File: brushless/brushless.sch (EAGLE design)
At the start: 71 parts, among them Q1 BUK7Y12-40E, Q2 BUK7Y12-40E, Q3 BUK7Y12-40E, Q4 BUK7Y12-40E, Q5 BUK7Y12-40E, Q6 BUK7Y12-40E, X2 MOTOR

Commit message: 0.25
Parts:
- UC1: device stm32:STM32F103CB -> rhoban:STM32_STM32F103CB
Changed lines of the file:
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@@
 <attribute name="FARNELL" value="1581233"/>
 </part>
-<part name="UC1" library="stm32" deviceset="STM32F103CB" device="" value="STM32F103CBT6">
+<part name="UC1" library="rhoban" deviceset="STM32_STM32F103CB" device="" value="STM32F103CBT6">
 <attribute name="FARNELL" value="1606327"/>
 </part>

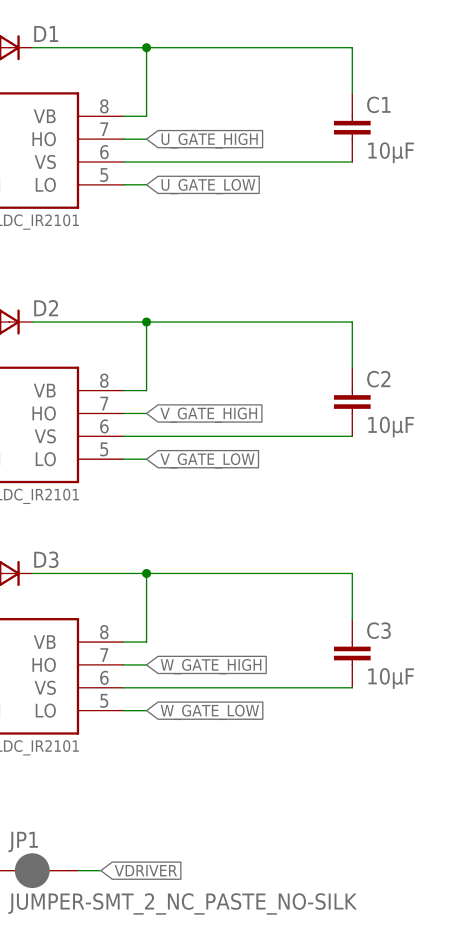
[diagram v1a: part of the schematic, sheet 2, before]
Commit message: Fixing phase on bootstrap capcaitors
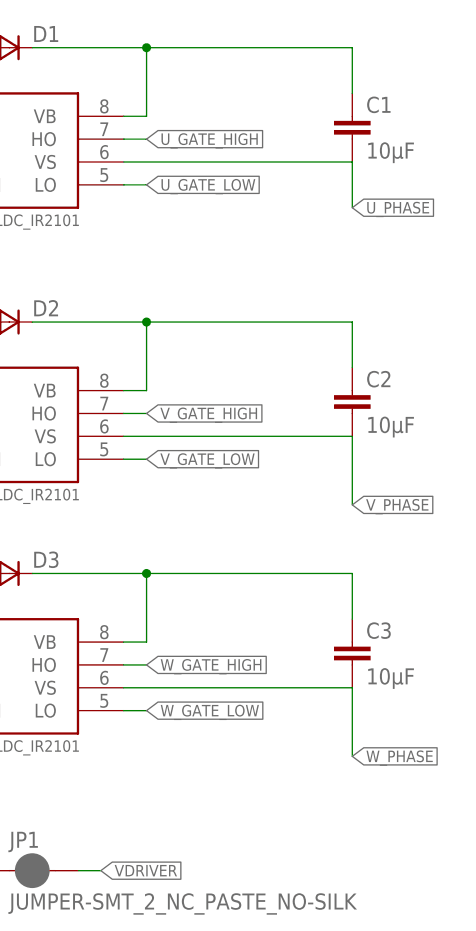
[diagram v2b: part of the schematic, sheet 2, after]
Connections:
- removed net N$11: C1.2, DRV1.VS
- removed net N$14: C2.2, DRV2.VS
- removed net N$18: C3.2, DRV3.VS
- net U_PHASE: now also C1.2, DRV1.VS
- net V_PHASE: now also C2.2, DRV2.VS
- net W_PHASE: now also C3.2, DRV3.VS
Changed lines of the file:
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@@
 </segment>
 </net>
-<net name="N$11" class="0">
+<net name="U_PHASE" class="2">
 <segment>
 <pinref part="C1" gate="G$1" pin="2"/>
 <pinref part="DRV1" gate="G$1" pin="VS"/>
 <wire x1="88.9" y1="78.74" x2="63.5" y2="78.74" width="0.1524" layer="91"/>
+<wire x1="88.9" y1="78.74" x2="88.9" y2="73.66" width="0.1524" layer="91"/>
+<label x="88.9" y="73.66" size="1.27" layer="95" xref="yes"/>
 </segment>
 </net>
@@
 </segment>
 </net>
-<net name="N$14" class="0">
+<net name="V_PHASE" class="2">
 <segment>
 <pinref part="C2" gate="G$1" pin="2"/>
 <pinref part="DRV2" gate="G$1" pin="VS"/>
 <wire x1="88.9" y1="48.26" x2="63.5" y2="48.26" width="0.1524" layer="91"/>
+<wire x1="88.9" y1="48.26" x2="88.9" y2="40.64" width="0.1524" layer="91"/>
+<label x="88.9" y="40.64" size="1.27" layer="95" xref="yes"/>
 </segment>
 </net>
@@
 </segment>
 </net>
-<net name="N$18" class="0">
+<net name="W_PHASE" class="2">
 <segment>
 <pinref part="C3" gate="G$1" pin="2"/>
 <pinref part="DRV3" gate="G$1" pin="VS"/>
 <wire x1="88.9" y1="20.32" x2="63.5" y2="20.32" width="0.1524" layer="91"/>
+<wire x1="88.9" y1="20.32" x2="88.9" y2="12.7" width="0.1524" layer="91"/>
+<label x="88.9" y="12.7" size="1.27" layer="95" xref="yes"/>
 </segment>
 </net>

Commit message: Changing ref for cap 100uF (fixes #18)
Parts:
- C10: FARNELL 1144713 -> 1870964
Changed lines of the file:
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@@
 </part>
 <part name="C10" library="rhoban" deviceset="CPOL_EU" device="_3.5-8" value="100uF">
-<attribute name="FARNELL" value="1144713"/>
+<attribute name="FARNELL" value="1870964"/>
 </part>
 <part name="D5" library="SparkFun-DiscreteSemi" deviceset="DIODE" device="SOD">

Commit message: Updating designs
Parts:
- removed R13, R22, R26: 10K, SparkFun-Resistors:RESISTOR0805
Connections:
- net GND: no longer R13.1, R14.1, R17.1, R18.1, R22.1, R26.1
- net HALLU: no longer R26.2
- net HALLV: no longer R22.2
- net HALLW: no longer R13.2
- net N$1: now also R14.2
- net N$2: now also R17.2
- net N$7: now also R18.2
- net U_GATE_HIGH: no longer R14.2
- net U_PHASE: now also R14.1
- net V_GATE_HIGH: no longer R17.2
- net V_PHASE: now also R17.1
- net W_GATE_HIGH: no longer R18.2
- net W_PHASE: now also R18.1
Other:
- moved on the sheet: R1, R14, R15, R16, R17, R18, R19, R3, R5

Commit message: Updating BOMs and ATTRs
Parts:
- ENCODER, HALL, X2: FARNELL (none) -> -
- K1: FARNELL (none) -> 2470821
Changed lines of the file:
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@@
 <attribute name="FARNELL" value="-"/>
 </part>
-<part name="K1" library="rhoban" deviceset="614105150721" device=""/>
-<part name="X2" library="Rembrandt Electronics - JST XH Connectors v1-0" deviceset="JST-XH-03-PIN" device="-LONG-PAD" value="MOTOR"/>
-<part name="HALL" library="jst" deviceset="B5B-ZR" device=""/>
-<part name="ENCODER" library="jst" deviceset="B6B-ZR" device=""/>
+<part name="K1" library="rhoban" deviceset="614105150721" device="">
+<attribute name="FARNELL" value="2470821"/>
+</part>
+<part name="X2" library="Rembrandt Electronics - JST XH Connectors v1-0" deviceset="JST-XH-03-PIN" device="-LONG-PAD" value="MOTOR">
+<attribute name="FARNELL" value="-"/>
+</part>
+<part name="HALL" library="jst" deviceset="B5B-ZR" device="">
+<attribute name="FARNELL" value="-"/>
+</part>
+<part name="ENCODER" library="jst" deviceset="B6B-ZR" device="">
+<attribute name="FARNELL" value="-"/>
+</part>
 <part name="D6" library="SparkFun-DiscreteSemi" deviceset="DIODE" device="SOD">
 <attribute name="FARNELL" value="8737843RL"/>
@@
 <attribute name="FARNELL" x="-40.64" y="-55.88" size="1.27" layer="96" rot="R270" display="off"/>
 </instance>
-<instance part="K1" gate="G$1" x="-53.34" y="-48.26" rot="R180"/>
+<instance part="K1" gate="G$1" x="-53.34" y="-48.26" rot="R180">
+<attribute name="FARNELL" x="-53.34" y="-48.26" size="1.778" layer="96" rot="R180" display="off"/>
+</instance>
 </instances>
 <busses>
@@
 <attribute name="FARNELL" x="-15.24" y="-25.4" size="1.27" layer="96" display="off"/>
 </instance>
-<instance part="X2" gate="-1" x="-35.56" y="-40.64"/>
+<instance part="X2" gate="-1" x="-35.56" y="-40.64">
+<attribute name="FARNELL" x="-35.56" y="-40.64" size="1.778" layer="96" display="off"/>
+</instance>
 <instance part="X2" gate="-2" x="-35.56" y="-43.18"/>
 <instance part="X2" gate="-3" x="-35.56" y="-45.72"/>
-<instance part="HALL" gate="G$1" x="7.62" y="10.16"/>
-<instance part="ENCODER" gate="G$1" x="5.08" y="-5.08"/>
+<instance part="HALL" gate="G$1" x="7.62" y="10.16">
+<attribute name="FARNELL" x="7.62" y="10.16" size="1.778" layer="96" display="off"/>
+</instance>
+<instance part="ENCODER" gate="G$1" x="5.08" y="-5.08">
+<attribute name="FARNELL" x="5.08" y="-5.08" size="1.778" layer="96" display="off"/>
+</instance>
 <instance part="D6" gate="G$1" x="-15.24" y="-33.02">
 <attribute name="FARNELL" x="-15.24" y="-33.02" size="1.27" layer="96" display="off"/>

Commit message: Moving to IR2103
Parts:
- DRV1, DRV2, DRV3: FARNELL 2296000 -> 8638730
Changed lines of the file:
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@@
 </part>
 <part name="DRV1" library="rhoban" deviceset="OPEN-BLDC_IR2101" device="">
-<attribute name="FARNELL" value="2296000"/>
+<attribute name="FARNELL" value="8638730"/>
 </part>
 <part name="D1" library="rhoban" deviceset="ZETEX_VAR2SOT23" device="">
@@
 </part>
 <part name="DRV2" library="rhoban" deviceset="OPEN-BLDC_IR2101" device="">
-<attribute name="FARNELL" value="2296000"/>
+<attribute name="FARNELL" value="8638730"/>
 </part>
 <part name="D2" library="rhoban" deviceset="ZETEX_VAR2SOT23" device="">
@@
 </part>
 <part name="DRV3" library="rhoban" deviceset="OPEN-BLDC_IR2101" device="">
-<attribute name="FARNELL" value="2296000"/>
+<attribute name="FARNELL" value="8638730"/>
 </part>
 <part name="D3" library="rhoban" deviceset="ZETEX_VAR2SOT23" device="">

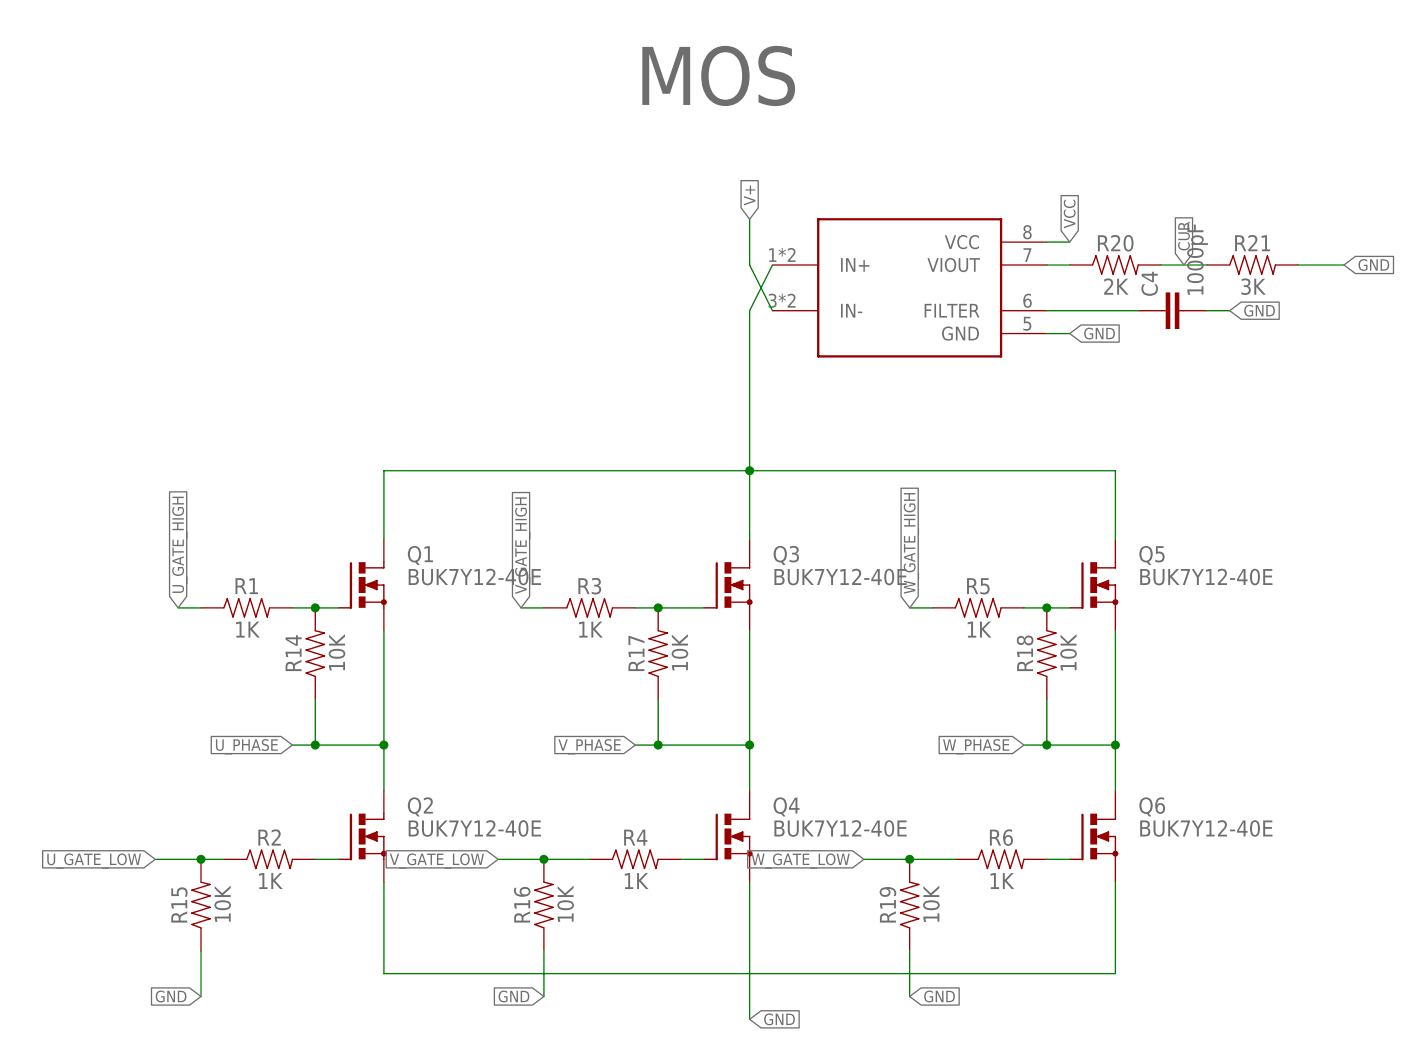
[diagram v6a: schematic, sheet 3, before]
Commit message: 10 ohms on mos gates
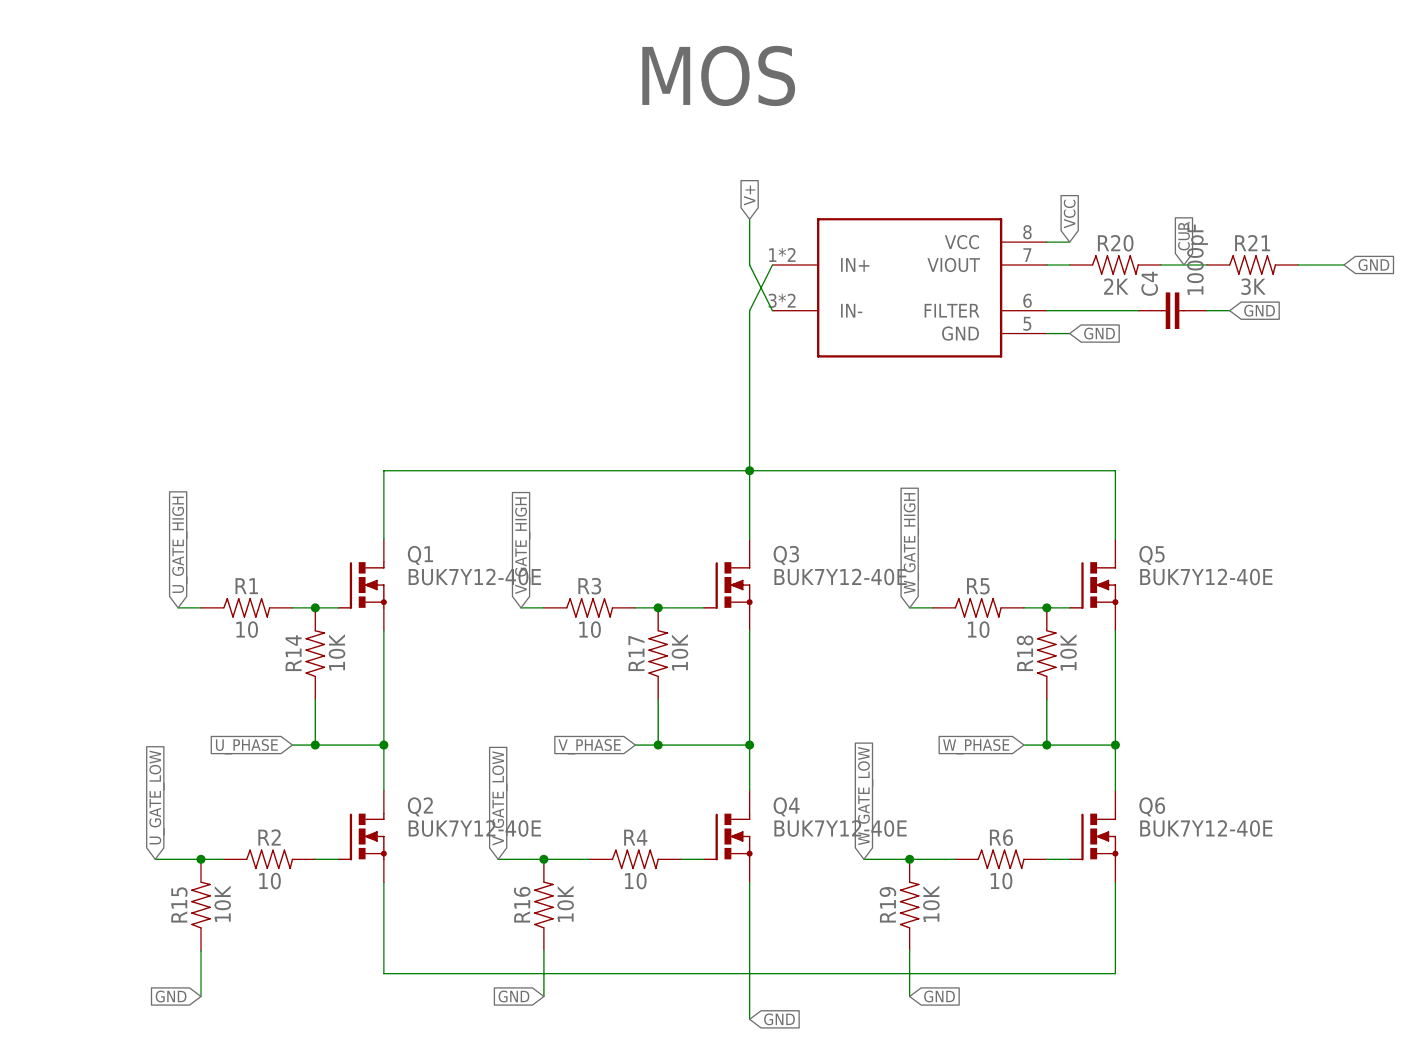
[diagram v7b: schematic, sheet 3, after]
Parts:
- R1, R2, R3, R4, R5, R6: value 1K -> 10
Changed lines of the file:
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@@
 <attribute name="FARNELL" value="2528772"/>
 </part>
-<part name="R1" library="SparkFun-Resistors" deviceset="RESISTOR" device="0805" value="1K">
+<part name="R1" library="SparkFun-Resistors" deviceset="RESISTOR" device="0805" value="10">
 <attribute name="FARNELL" value="2446904"/>
 </part>
-<part name="R2" library="SparkFun-Resistors" deviceset="RESISTOR" device="0805" value="1K">
+<part name="R2" library="SparkFun-Resistors" deviceset="RESISTOR" device="0805" value="10">
 <attribute name="FARNELL" value="2446904"/>
 </part>
-<part name="R3" library="SparkFun-Resistors" deviceset="RESISTOR" device="0805" value="1K">
+<part name="R3" library="SparkFun-Resistors" deviceset="RESISTOR" device="0805" value="10">
 <attribute name="FARNELL" value="2446904"/>
 </part>
-<part name="R4" library="SparkFun-Resistors" deviceset="RESISTOR" device="0805" value="1K">
+<part name="R4" library="SparkFun-Resistors" deviceset="RESISTOR" device="0805" value="10">
 <attribute name="FARNELL" value="2446904"/>
 </part>
-<part name="R5" library="SparkFun-Resistors" deviceset="RESISTOR" device="0805" value="1K">
+<part name="R5" library="SparkFun-Resistors" deviceset="RESISTOR" device="0805" value="10">
 <attribute name="FARNELL" value="2446904"/>
 </part>
-<part name="R6" library="SparkFun-Resistors" deviceset="RESISTOR" device="0805" value="1K">
+<part name="R6" library="SparkFun-Resistors" deviceset="RESISTOR" device="0805" value="10">
 <attribute name="FARNELL" value="2446904"/>
 </part>
@@
 <pinref part="R2" gate="G$1" pin="1"/>
 <wire x1="12.7" y1="17.78" x2="10.16" y2="17.78" width="0.1524" layer="91"/>
-<label x="5.08" y="17.78" size="1.27" layer="95" rot="R180" xref="yes"/>
+<label x="5.08" y="17.78" size="1.27" layer="95" rot="R90" xref="yes"/>
 <pinref part="R15" gate="G$1" pin="2"/>
 <wire x1="10.16" y1="17.78" x2="5.08" y2="17.78" width="0.1524" layer="91"/>
@@
 <pinref part="R4" gate="G$1" pin="1"/>
 <wire x1="53.34" y1="17.78" x2="48.26" y2="17.78" width="0.1524" layer="91"/>
-<label x="43.18" y="17.78" size="1.27" layer="95" rot="R180" xref="yes"/>
+<label x="43.18" y="17.78" size="1.27" layer="95" rot="R90" xref="yes"/>
 <pinref part="R16" gate="G$1" pin="2"/>
 <wire x1="48.26" y1="17.78" x2="43.18" y2="17.78" width="0.1524" layer="91"/>
@@
 <pinref part="R6" gate="G$1" pin="1"/>
 <wire x1="93.98" y1="17.78" x2="88.9" y2="17.78" width="0.1524" layer="91"/>
-<label x="83.82" y="17.78" size="1.27" layer="95" rot="R180" xref="yes"/>
+<label x="83.82" y="17.78" size="1.27" layer="95" rot="R90" xref="yes"/>
 <pinref part="R19" gate="G$1" pin="2"/>
 <wire x1="88.9" y1="17.78" x2="83.82" y2="17.78" width="0.1524" layer="91"/>

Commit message: schematic modified on brushless board
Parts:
- removed R14, R15, R16, R17, R18, R19: 10K, SparkFun-Resistors:RESISTOR0805
- added C11, C13, C9: 1000pF, SparkFun-Passives:CAP0805
- added C5, C6, C8: 1uF, SparkFun-Passives:CAP0805
- added D10, D11, D12, D7, D8, D9: (no value), SparkFun-DiscreteSemi:DIODESOD
- D1, D2, D3: device rhoban:ZETEX_VAR2SOT23 -> SparkFun-DiscreteSemi:DIODESOD; FARNELL 2317446 -> 8737843RL
- R10, R11, R12, R7, R8, R9: value 10K -> 10; FARNELL 2447553 -> 2446904; PROD_ID (none) -> (none); VALUE (none) -> (none)
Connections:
- removed net 3.3: C12.2, C7.2, LOGIC.3, R40.1, R49.1, REG1.OUT, UC1.VDD_1, UC1.VDD_2, UC1.VDD_3, UC1.VDD_A
- removed net GND: C10.-, C12.1, C20.1, C21.1, C4.2, C7.1, D4.C, DRV1.COM, DRV2.COM, DRV3.COM, ENCODER.1, GND.1, GND.2, GND.3, HALL.1, K1.5GND, K1.GND@1, K1.GND@2, LOGIC.1, Q2.S, Q4.S, Q6.S, R15.1, R16.1, R19.1, R21.2, R39.2, R48.2, R50.1, REG1.GND, SENSE.GND, UC1.VSS_1, UC1.VSS_2, UC1.VSS_3, UC1.VSS_A
- removed net N$1 (its old number): Q1.G, R1.2, R14.2
- removed net W_GATE_HIGH: DRV3.HO, R5.1
- removed net W_GATE_LOW: DRV3.LO, R19.2, R6.1
- new net +3V3: C11.1, C12.2, C7.2, LOGIC.3, R40.1, R49.1, REG1.OUT, UC1.VDD_1, UC1.VDD_2, UC1.VDD_3, UC1.VDD_A
- new net AGND: C10.-, C11.2, C12.1, C13.2, C20.1, C21.1, C4.2, C5.1, C6.1, C7.1, C8.1, C9.2, D4.C, DRV1.COM, DRV2.COM, DRV3.COM, ENCODER.1, GND.1, GND.2, GND.3, HALL.1, K1.5GND, K1.GND@1, K1.GND@2, LOGIC.1, Q2.S, Q4.S, Q6.S, R21.2, R39.2, R48.2, R50.1, REG1.GND, SENSE.GND, UC1.VSS_1, UC1.VSS_2, UC1.VSS_3, UC1.VSS_A
- new net N$11: D1.A, Q1.G, R1.2
- new net N$12: D10.C, DRV3.HO, R5.1
- new net N$13: D11.C, DRV3.LO, R6.1
- new net VUSB1: D12.A
- net N$2: now also D7.A; no longer R17.2
- net N$22: now also C13.1, D12.C; no longer D6.C
- net N$3: now also D9.A
- net N$5: now also D6.C; no longer D1.C
- net N$6: now also D8.A
- net N$7: now also D10.A; no longer R18.2
- net N$9: now also D11.A
- net U_GATE_HIGH: now also D1.C
- net U_GATE_LOW: now also D9.C; no longer R15.2
- net U_PHASE: no longer R14.1
- net VCC: now also C9.1
- net VDRIVER: now also C5.2, C6.2, C8.2, D6.A; no longer D1.A
- net VUSB: no longer D6.A
- net V_GATE_HIGH: now also D7.C
- net V_GATE_LOW: now also D8.C; no longer R16.2
- net V_PHASE: no longer R17.1
- net W_PHASE: no longer R18.1
